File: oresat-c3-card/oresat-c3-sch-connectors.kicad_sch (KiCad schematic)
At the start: 28 parts, among them J1 TFM-120-01-L-D-RA, J3 733000020, J4 733000020, J8 SM14B-SHLS-TF

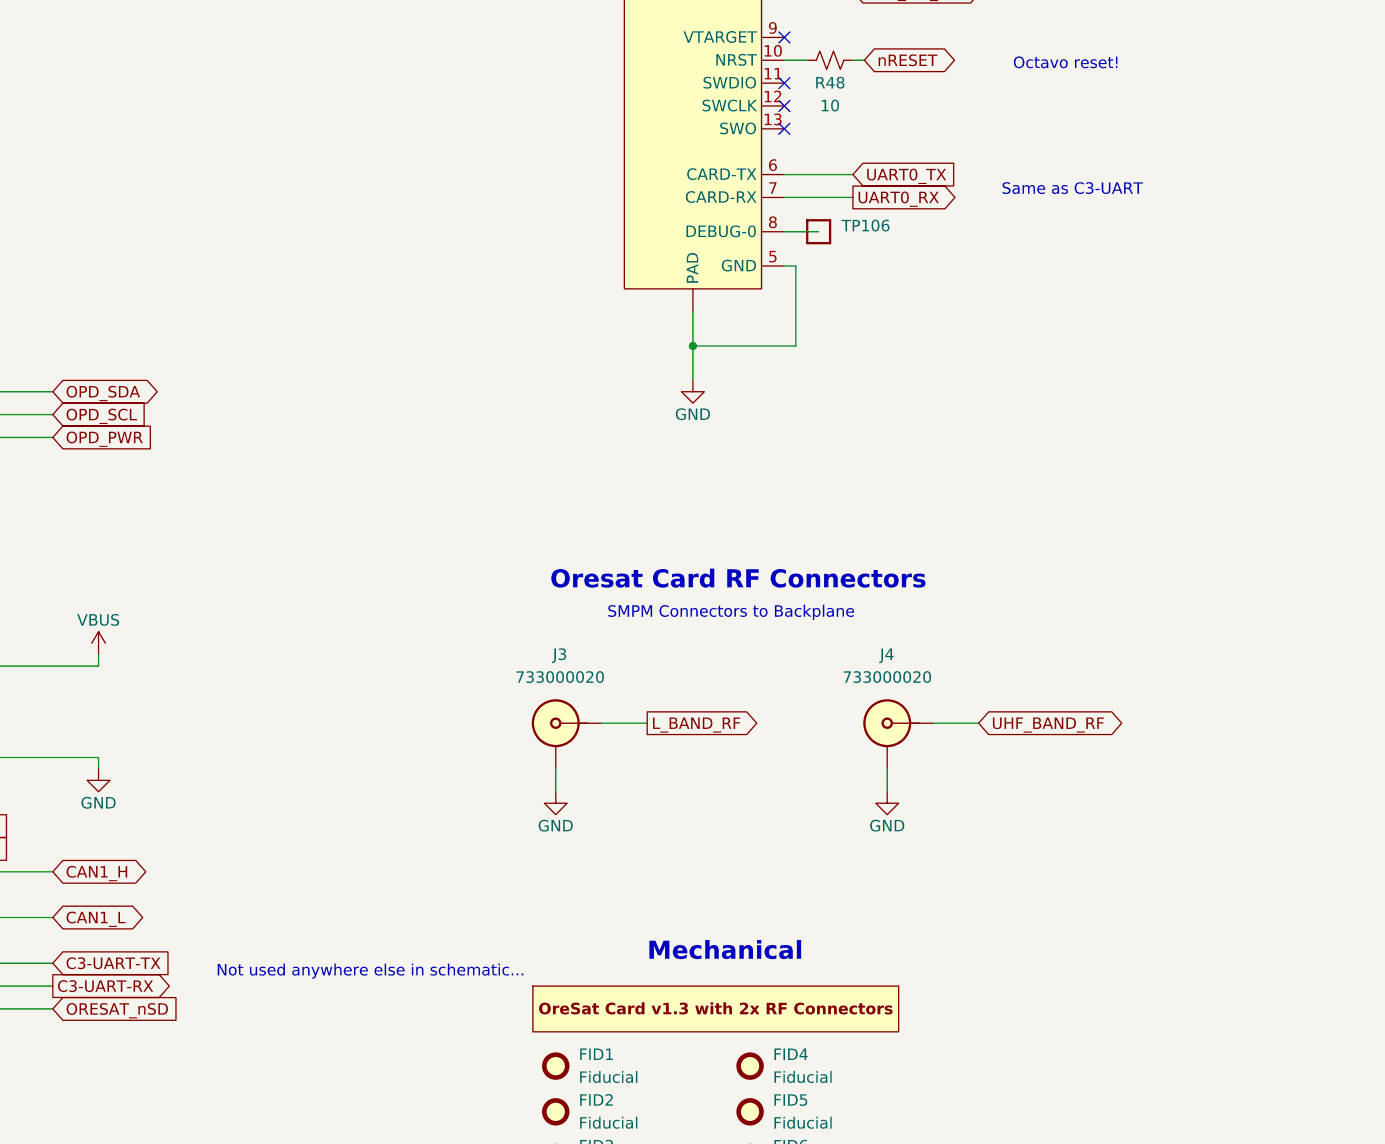
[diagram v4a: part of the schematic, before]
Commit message: finished connecting and routing, starting on clean up
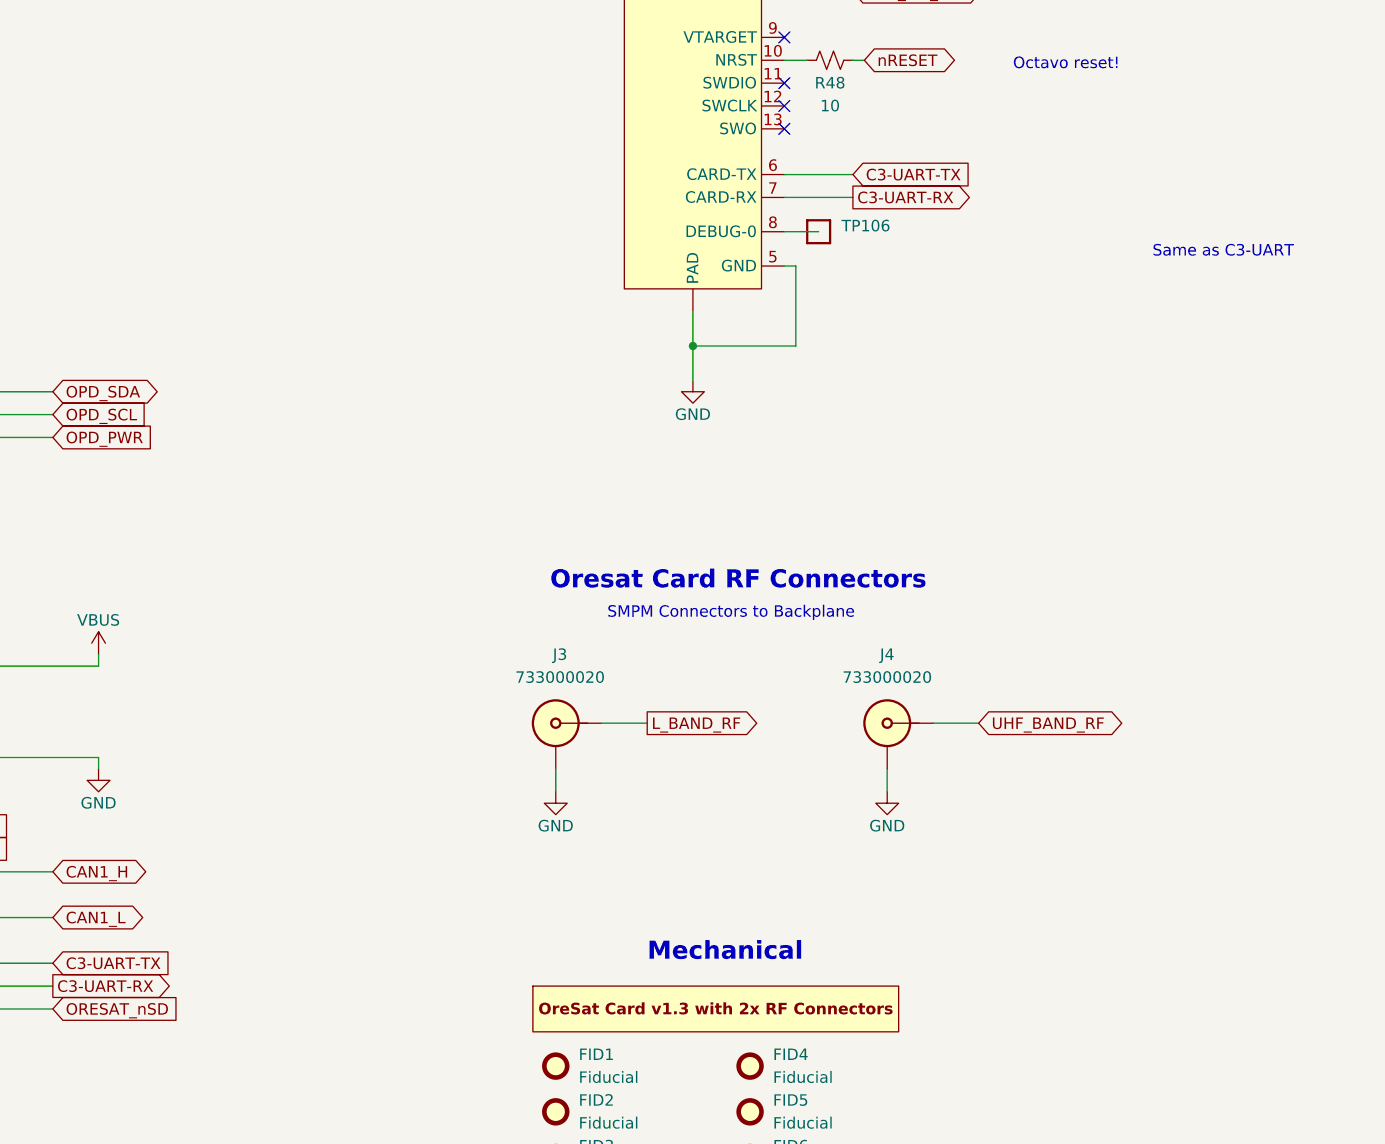
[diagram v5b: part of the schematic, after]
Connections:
- net UART0_RX is gone; now on net C3-UART-RX: J8.7 (CARD-RX)
- net UART0_TX is gone; now on net C3-UART-TX: J8.6 (CARD-TX)
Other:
- note removed: "Not used anywhere else in schematic..."
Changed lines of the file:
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@@
-		)
-	)
-	(text "Not used anywhere else in schematic..."
-		(exclude_from_sim no)
-		(at 176.276 188.976 0)
-		(effects
-			(font
-				(size 1.27 1.27)
-			)
 		)
 	)
@@
 	(text "Same as C3-UART"
 		(exclude_from_sim no)
-		(at 246.38 102.87 0)
+		(at 263.144 109.728 0)
 		(effects
 			(font
@@
 		)
 	)
-	(global_label "UART0_TX"
-		(shape input)
-		(at 229.87 100.33 0)
+	(global_label "C3-UART-RX"
+		(shape output)
+		(at 229.87 102.87 0)
 		(fields_autoplaced yes)
 		(effects
@@
 		)
 		(property "Intersheetrefs" "${INTERSHEET_REFS}"
-			(at 241.7867 100.33 0)
+			(at 245.6157 102.87 0)
 			(effects
 				(font
@@
 		)
 	)
-	(global_label "UART0_RX"
-		(shape output)
-		(at 229.87 102.87 0)
-		(fields_autoplaced yes)
-		(effects
-			(font
-				(size 1.27 1.27)
-			)
-			(justify left)
-		)
-		(property "Intersheetrefs" "${INTERSHEET_REFS}"
-			(at 242.0891 102.87 0)
-			(effects
-				(font
-					(size 1.27 1.27)
-				)
-				(justify left)
-			)
-		)
-	)
 	(global_label "CAN2_L"
 		(shape input)
@@
 			(effects
 				(font
+					(size 1.27 1.27)
+				)
+				(justify left)
+			)
+		)
+	)
+	(global_label "C3-UART-TX"
+		(shape input)
+		(at 229.87 100.33 0)
+		(fields_autoplaced yes)
+		(effects
+			(font
+				(size 1.27 1.27)
+			)
+			(justify left)
+		)
+		(property "Intersheetrefs" "${INTERSHEET_REFS}"
+			(at 245.3133 100.33 0)
+			(effects
+				(font

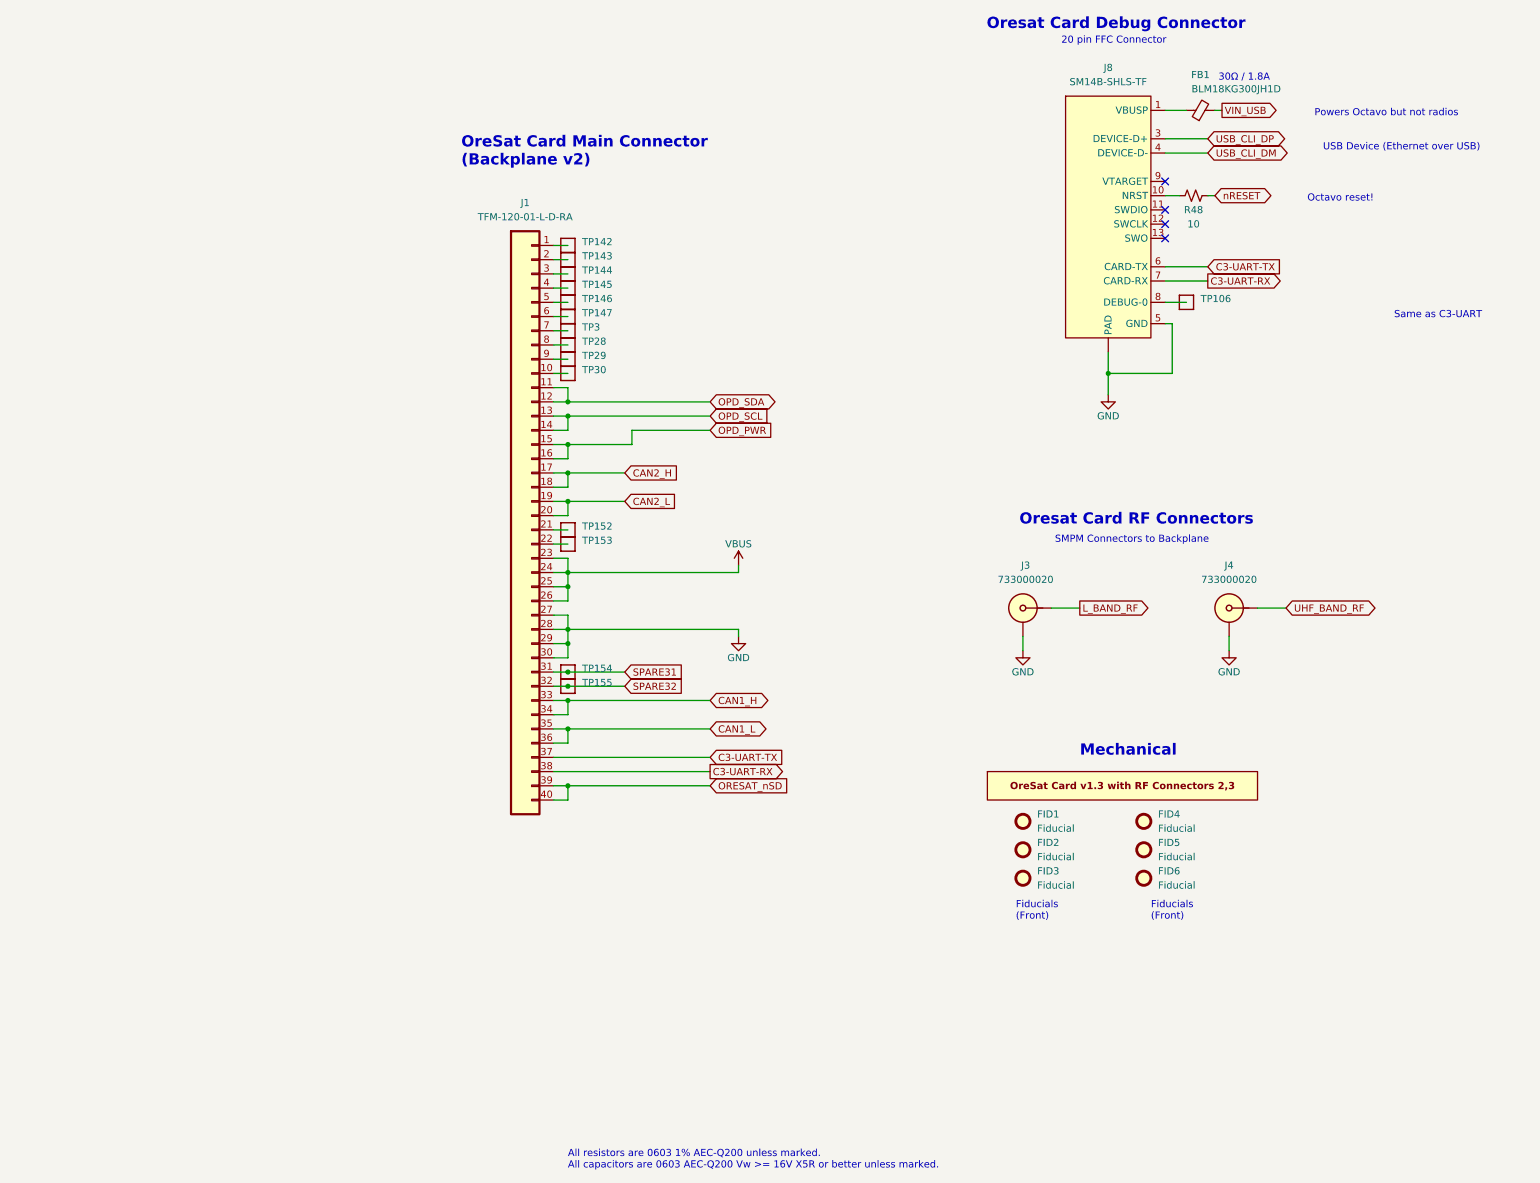
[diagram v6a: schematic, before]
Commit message: Design review on C3 v7.0
Glenn and Andrew did a design review. Removed fiducials on back of board. Lots of schematic fixes, including
direction connection of TCXOs to AT86s, corrected LPF of CLKO from AT86 to the synth reference, fixed drive
levels both QPC switches in UHF radio, confirmed QPC directions, and some minor polishing.
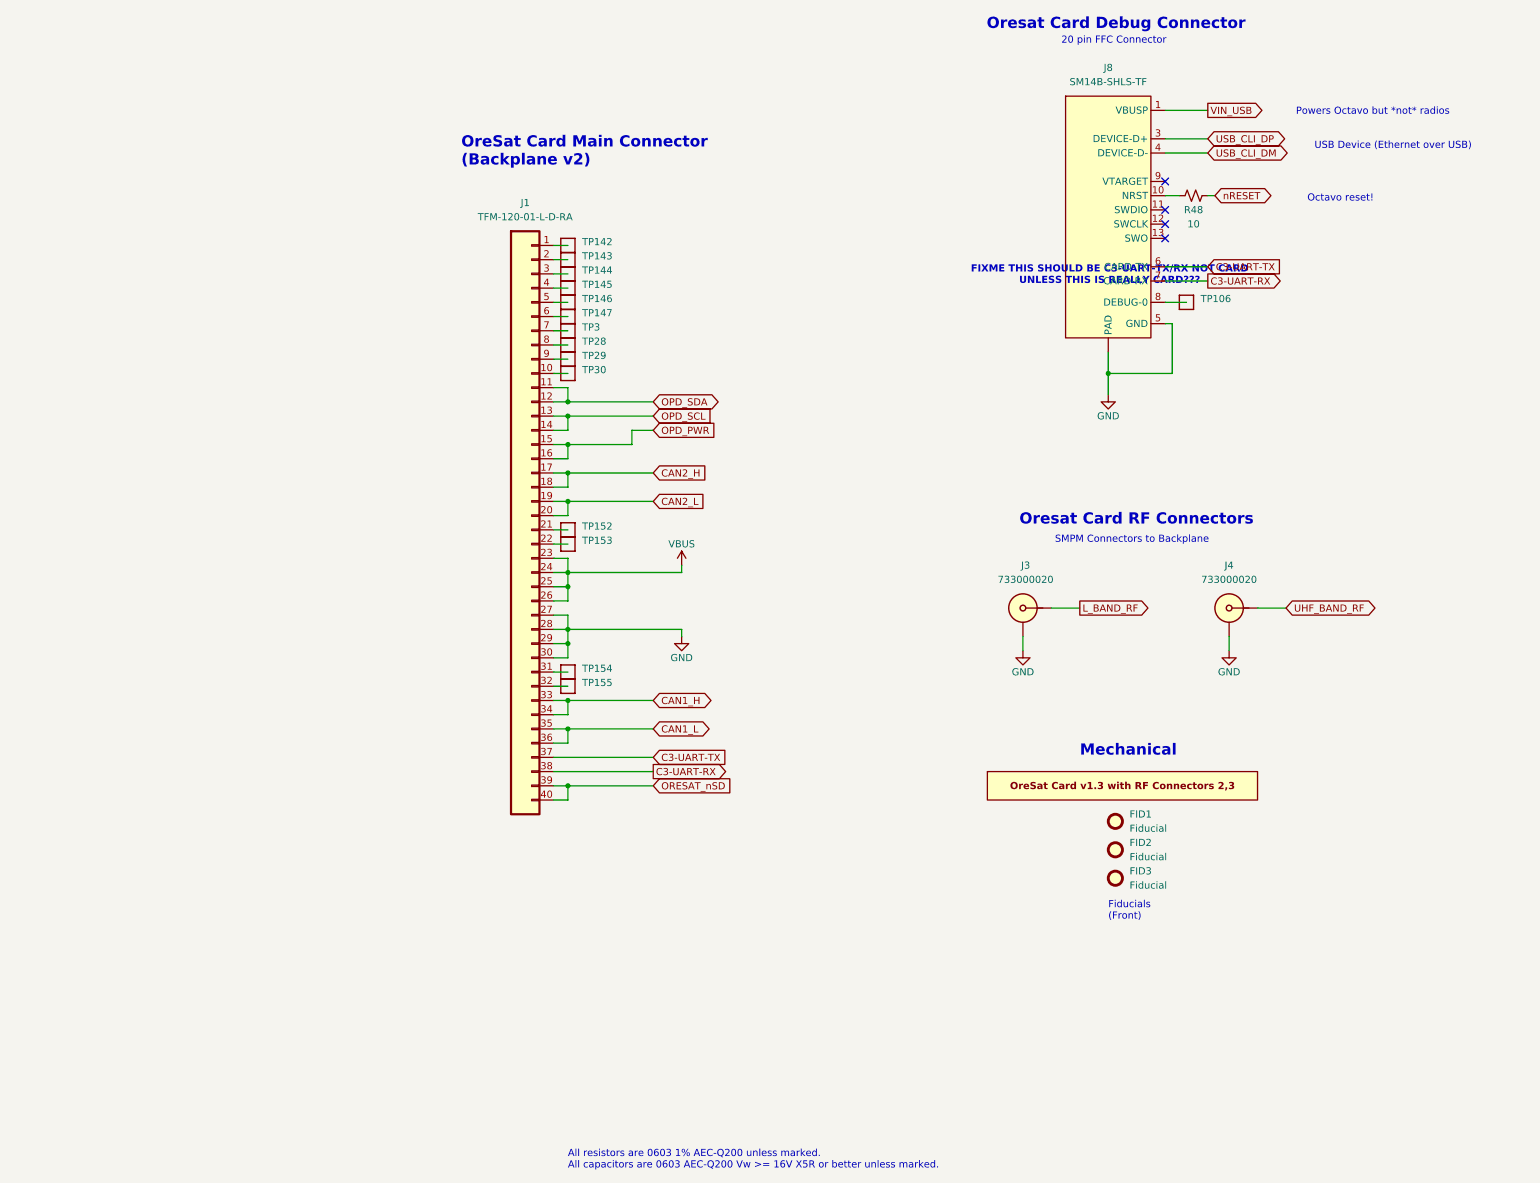
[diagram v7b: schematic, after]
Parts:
- removed FB1: BLM18KG300JH1D, Inductor_SMD:L_0603_1608Metric, symbol Device:FerriteBead_Small
- removed FID4, FID5, FID6: Fiducial, Fiducial:Fiducial_1mm_Mask2mm, symbol Mechanical:Fiducial
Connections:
- net VIN_USB: now also J8.1 (VBUSP), J8.2 (VBUSP)
- net SPARE31: no longer names the net of J1.31, TP154.1
- net SPARE32: no longer names the net of J1.32, TP155.1
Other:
- note added: "FIXME THIS SHOULD BE C3-UART-TX/RX NOT CARD UNLESS THIS IS REALLY CARD???"
- note added: "Powers Octavo but *not* radios"
- note removed: "30Ω / 1.8A"
- note removed: "Powers Octavo but not radios"
- note removed: "Same as C3-UART"
- moved on the sheet: FID1, FID2, FID3
